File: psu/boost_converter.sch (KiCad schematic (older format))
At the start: 89 parts

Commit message: update psu
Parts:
- gave numbers to parts that had none: 89

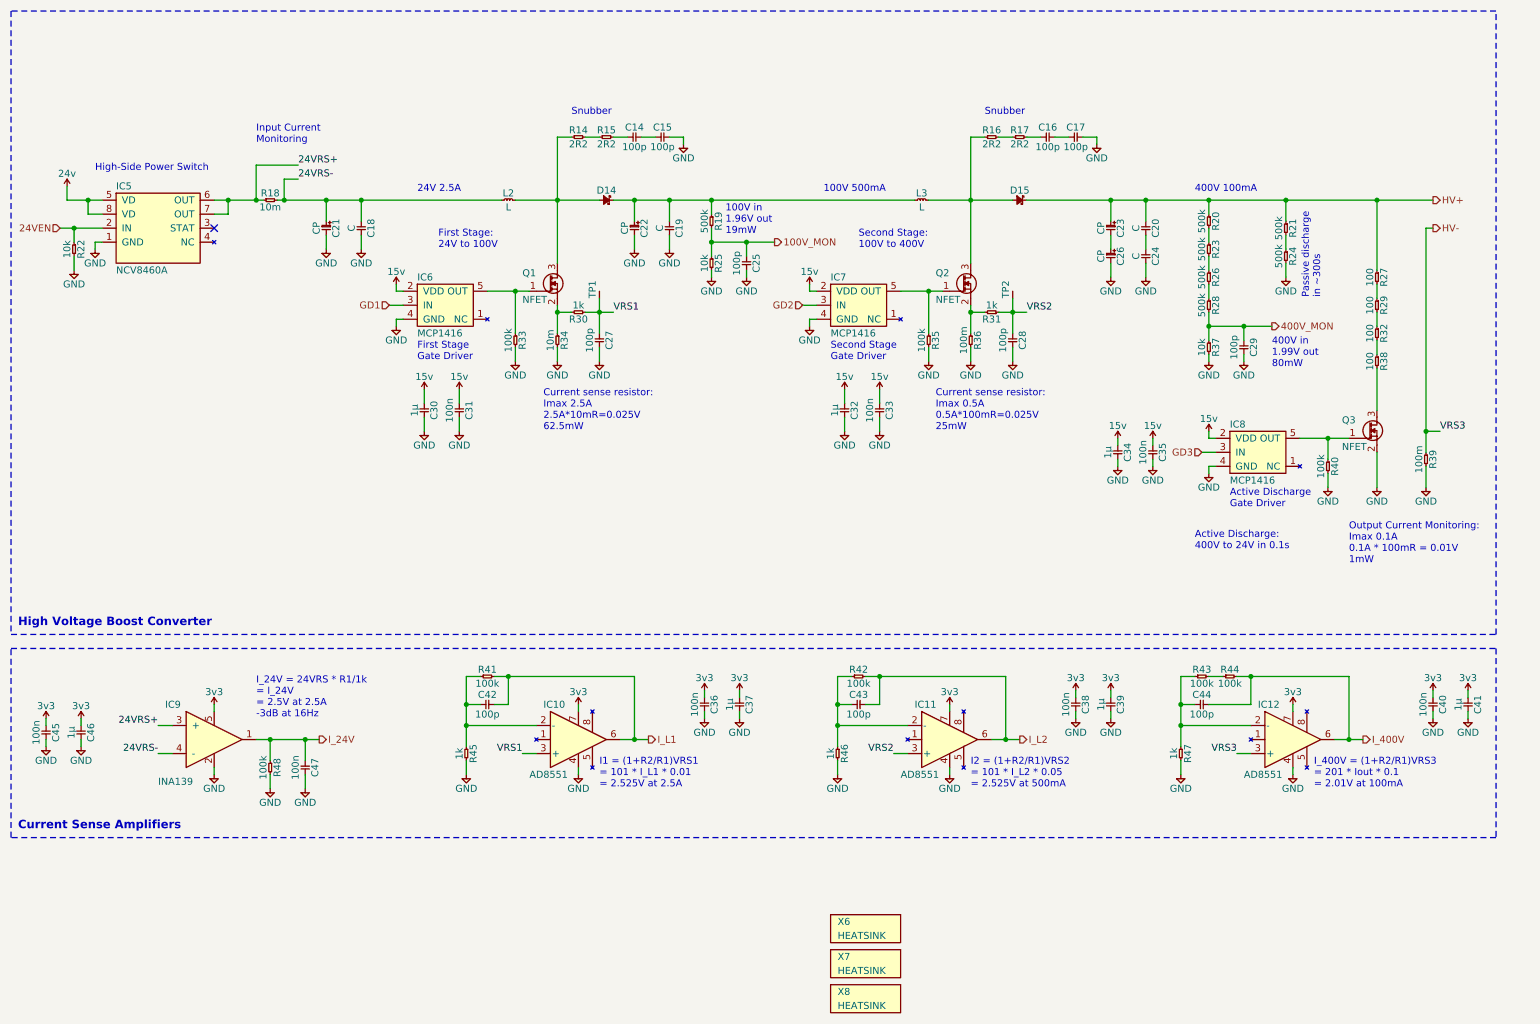
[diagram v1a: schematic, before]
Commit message: assign diodes and main transistors
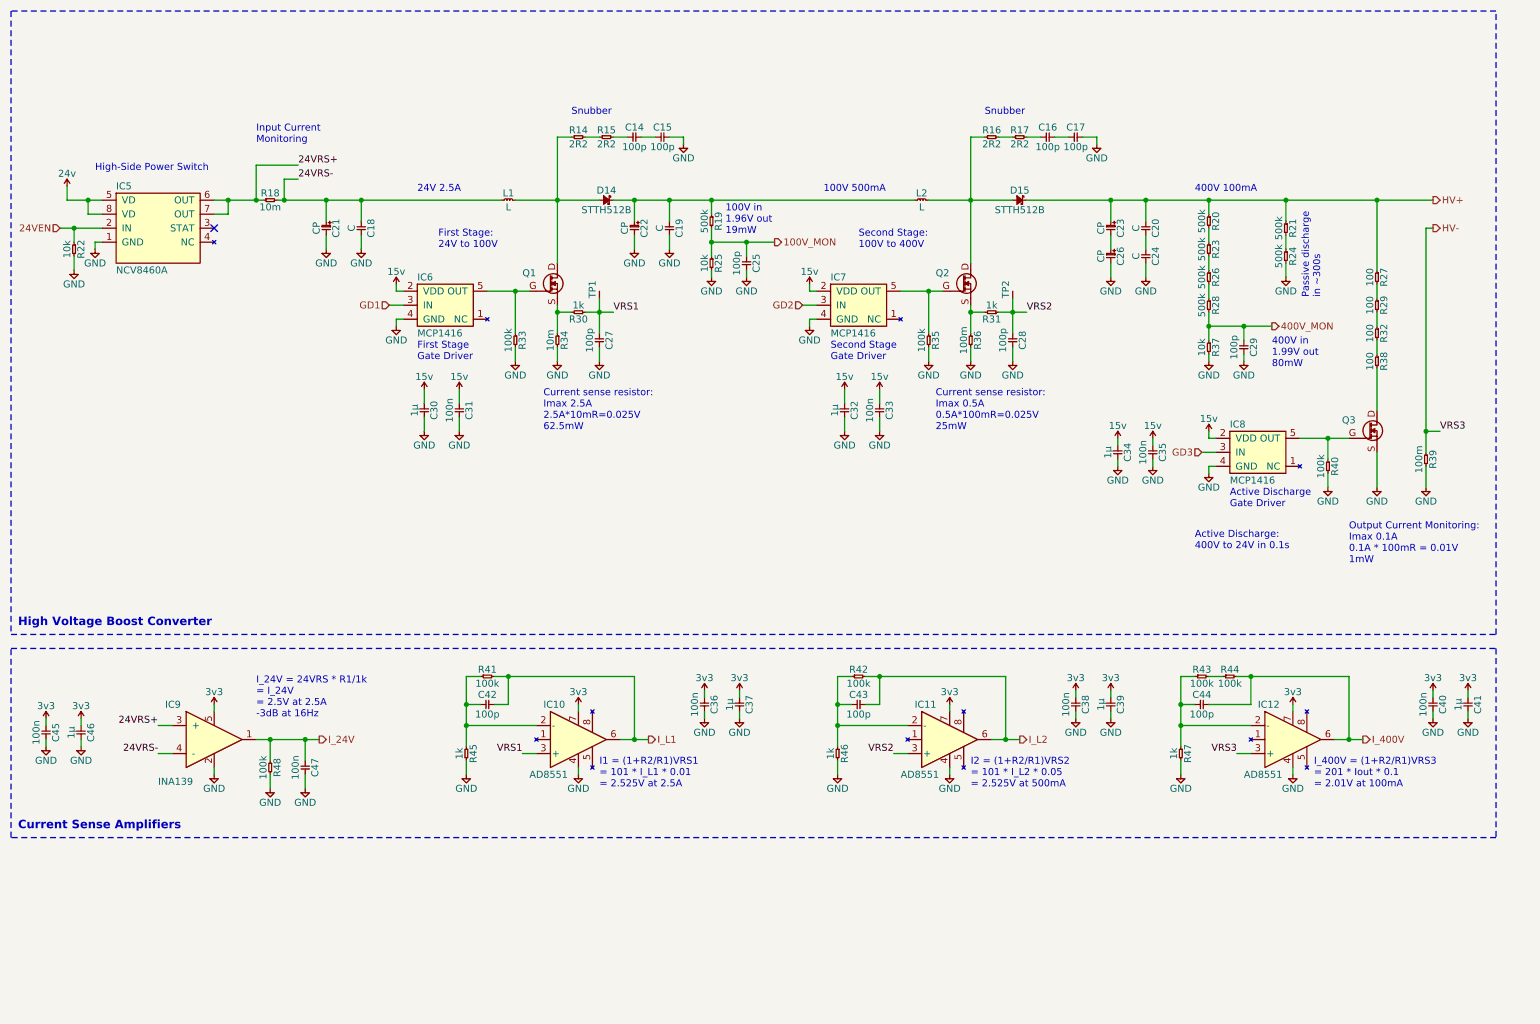
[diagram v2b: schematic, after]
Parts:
- removed Q1, Q2, Q3: NFET, symbol agg:NFET
- removed X6, X7, X8: HEATSINK, symbol agg:PART
- added Q1, Q2, Q3: STB45N60DM2AG, agg:D2PAK_GDS, symbol agg:NFET_GDS
- D14, D15: value SCHOTTKY -> STTH512B; footprint (none) -> agg:DPAK_DIODE; Farnell (none) -> 2344055
- renumbered L2 to L1, L3 to L2
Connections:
- net GND: now also Q3.S
- net at IC6.5 (OUT), R33.1: now also Q1.G
- net at IC7.5 (OUT), R35.1: now also Q2.G
- net at R30.2, R34.1: now also Q1.S
- net at D14.2, L1.2, R14.1: now also Q1.D
- net at R31.2, R36.1: now also Q2.S
- net at D15.2, L2.2, R16.1: now also Q2.D
- net at IC8.5 (OUT), R40.1: now also Q3.G
- net at R38.2: now also Q3.D
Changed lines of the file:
@@
 	6300 2650 6200 2650
-$Comp
-L agg:NFET Q?
-U 1 1 614C6078
-P 4450 2450
-AR Path="/614C6078" Ref="Q?"  Part="1"
-AR Path="/6147A5D5/614C6078" Ref="Q1"  Part="1"
-F 0 "Q1" H 4200 2480 50  0000 L CNN
-F 1 "NFET" H 4200 2290 50  0000 L CNN
-F 2 "" H 4450 2450 50  0001 C CNN
-F 3 "" H 4450 2450 50  0001 C CNN
-	1    4450 2450
-	1    0    0    -1
-$EndComp
 $Comp
 L agg:R R?
@@
 Wire Wire Line
 	4150 2550 4250 2550
-$Comp
-L agg:NFET Q?
-U 1 1 614C6088
-P 7400 2450
-AR Path="/614C6088" Ref="Q?"  Part="1"
-AR Path="/6147A5D5/614C6088" Ref="Q2"  Part="1"
-F 0 "Q2" H 7150 2480 50  0000 L CNN
-F 1 "NFET" H 7150 2290 50  0000 L CNN
-F 2 "" H 7400 2450 50  0001 C CNN
-F 3 "" H 7400 2450 50  0001 C CNN
-	1    7400 2450
-	1    0    0    -1
-$EndComp
 $Comp
 L agg:R R?
@@
 P 4050 1900
 AR Path="/614C6132" Ref="L?"  Part="1"
-AR Path="/6147A5D5/614C6132" Ref="L2"  Part="1"
-F 0 "L2" H 4100 1950 50  0000 C CNN
+AR Path="/6147A5D5/614C6132" Ref="L1"  Part="1"
+F 0 "L1" H 4100 1950 50  0000 C CNN
 F 1 "L" H 4100 1850 50  0000 C CNN
 F 2 "" H 4050 1900 50  0001 C CNN
@@
 AR Path="/6147A5D5/614C615C" Ref="D14"  Part="1"
 F 0 "D14" H 4900 1970 50  0000 C CNN
-F 1 "SCHOTTKY" H 4900 1830 50  0001 C CNN
-F 2 "" H 4800 1870 50  0001 C CNN
-F 3 "" H 4900 1970 50  0001 C CNN
+F 1 "STTH512B" H 4900 1830 50  0000 C CNN
+F 2 "agg:DPAK_DIODE" H 4800 1870 50  0001 C CNN
+F 3 "https://www.st.com/resource/en/datasheet/stth512.pdf" H 4900 1970 50  0001 C CNN
+F 4 "2344055" H 4850 1900 50  0001 C CNN "Farnell"
 	1    4850 1900
 	-1   0    0    -1
@@
 P 7000 1900
 AR Path="/614C6176" Ref="L?"  Part="1"
-AR Path="/6147A5D5/614C6176" Ref="L3"  Part="1"
-F 0 "L3" H 7050 1950 50  0000 C CNN
+AR Path="/6147A5D5/614C6176" Ref="L2"  Part="1"
+F 0 "L2" H 7050 1950 50  0000 C CNN
 F 1 "L" H 7050 1850 50  0000 C CNN
 F 2 "" H 7000 1900 50  0001 C CNN
@@
 Wire Wire Line
 	7400 1900 7100 1900
-$Comp
-L agg:SCHOTTKY D?
-U 1 1 614C617E
-P 7800 1900
-AR Path="/614C617E" Ref="D?"  Part="1"
-AR Path="/6147A5D5/614C617E" Ref="D15"  Part="1"
-F 0 "D15" H 7850 1970 50  0000 C CNN
-F 1 "SCHOTTKY" H 7850 1830 50  0001 C CNN
-F 2 "" H 7750 1870 50  0001 C CNN
-F 3 "" H 7850 1970 50  0001 C CNN
-	1    7800 1900
-	-1   0    0    -1
-$EndComp
 Wire Wire Line
 	7700 1900 7400 1900
@@
 F 4 "1630421" H 9250 3200 50  0001 L CNN "Farnell"
 	1    9450 3700
-	1    0    0    -1
-$EndComp
-$Comp
-L agg:NFET Q?
-U 1 1 614C628B
-P 10300 3500
-AR Path="/614C628B" Ref="Q?"  Part="1"
-AR Path="/6147A5D5/614C628B" Ref="Q3"  Part="1"
-F 0 "Q3" H 10050 3530 50  0000 L CNN
-F 1 "NFET" H 10050 3340 50  0000 L CNN
-F 2 "" H 10300 3500 50  0001 C CNN
-F 3 "" H 10300 3500 50  0001 C CNN
-	1    10300 3500
 	1    0    0    -1
 $EndComp
@@
 Text Notes 600  6400 0    60   ~ 12
 Current Sense Amplifiers
-$Comp
-L agg:PART X?
-U 1 1 6297628F
-P 6400 7650
-AR Path="/6297628F" Ref="X?"  Part="1"
-AR Path="/6147A5D5/6297628F" Ref="X8"  Part="1"
-F 0 "X8" H 6450 7750 50  0000 L CNN
-F 1 "HEATSINK" H 6450 7650 50  0000 L CNN
-F 2 "" H 6400 7650 50  0001 C CNN
-F 3 "" H 6400 7650 50  0001 C CNN
-	1    6400 7650
-	1    0    0    -1
-$EndComp
-$Comp
-L agg:PART X?
-U 1 1 62976295
-P 6400 7400
-AR Path="/62976295" Ref="X?"  Part="1"
-AR Path="/6147A5D5/62976295" Ref="X7"  Part="1"
-F 0 "X7" H 6450 7500 50  0000 L CNN
-F 1 "HEATSINK" H 6450 7400 50  0000 L CNN
-F 2 "" H 6400 7400 50  0001 C CNN
-F 3 "" H 6400 7400 50  0001 C CNN
-	1    6400 7400
-	1    0    0    -1
-$EndComp
-$Comp
-L agg:PART X?
-U 1 1 629A6209
-P 6400 7150
-AR Path="/629A6209" Ref="X?"  Part="1"
-AR Path="/6147A5D5/629A6209" Ref="X6"  Part="1"
-F 0 "X6" H 6450 7250 50  0000 L CNN
-F 1 "HEATSINK" H 6450 7150 50  0000 L CNN
-F 2 "" H 6400 7150 50  0001 C CNN
-F 3 "" H 6400 7150 50  0001 C CNN
-	1    6400 7150
-	1    0    0    -1
-$EndComp
 Wire Notes Line
 	550  5000 11150 5000
@@
 Wire Wire Line
 	8150 5550 8150 5600
+$Comp
+L agg:SCHOTTKY D?
+U 1 1 62C4FC38
+P 7800 1900
+AR Path="/62C4FC38" Ref="D?"  Part="1"
+AR Path="/6147A5D5/62C4FC38" Ref="D15"  Part="1"
+F 0 "D15" H 7850 1970 50  0000 C CNN
+F 1 "STTH512B" H 7850 1830 50  0000 C CNN
+F 2 "agg:DPAK_DIODE" H 7750 1870 50  0001 C CNN
+F 3 "https://www.st.com/resource/en/datasheet/stth512.pdf" H 7850 1970 50  0001 C CNN
+F 4 "2344055" H 7800 1900 50  0001 C CNN "Farnell"
+	1    7800 1900
+	-1   0    0    -1
+$EndComp
+$Comp
+L agg:NFET_GDS Q1
+U 1 1 62C5D73E
+P 4450 2450
+F 0 "Q1" H 4200 2480 50  0000 L CNN
+F 1 "STB45N60DM2AG" H 4365 2285 50  0001 R CNN
+F 2 "agg:D2PAK_GDS" H 4450 2450 50  0001 C CNN
+F 3 "https://www.st.com/resource/en/datasheet/stb45n60dm2ag.pdf" H 4450 2450 50  0001 C CNN
+F 4 "3129762" H 4450 2450 50  0001 C CNN "Farnell"
+	1    4450 2450
+	1    0    0    -1
+$EndComp
+$Comp
+L agg:NFET_GDS Q2
+U 1 1 62C5E943
+P 7400 2450
+F 0 "Q2" H 7150 2480 50  0000 L CNN
+F 1 "STB45N60DM2AG" H 7315 2285 50  0001 R CNN
+F 2 "agg:D2PAK_GDS" H 7400 2450 50  0001 C CNN
+F 3 "https://www.st.com/resource/en/datasheet/stb45n60dm2ag.pdf" H 7400 2450 50  0001 C CNN
+F 4 "3129762" H 7400 2450 50  0001 C CNN "Farnell"
+	1    7400 2450
+	1    0    0    -1
+$EndComp
+$Comp
+L agg:NFET_GDS Q3
+U 1 1 62C60334
+P 10300 3500
+F 0 "Q3" H 10050 3530 50  0000 L CNN
+F 1 "STB45N60DM2AG" H 10215 3335 50  0001 R CNN
+F 2 "agg:D2PAK_GDS" H 10300 3500 50  0001 C CNN
+F 3 "https://www.st.com/resource/en/datasheet/stb45n60dm2ag.pdf" H 10300 3500 50  0001 C CNN
+F 4 "3129762" H 10300 3500 50  0001 C CNN "Farnell"
+	1    10300 3500
+	1    0    0    -1
+$EndComp
 $EndSCHEMATC

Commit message: Select main L and C
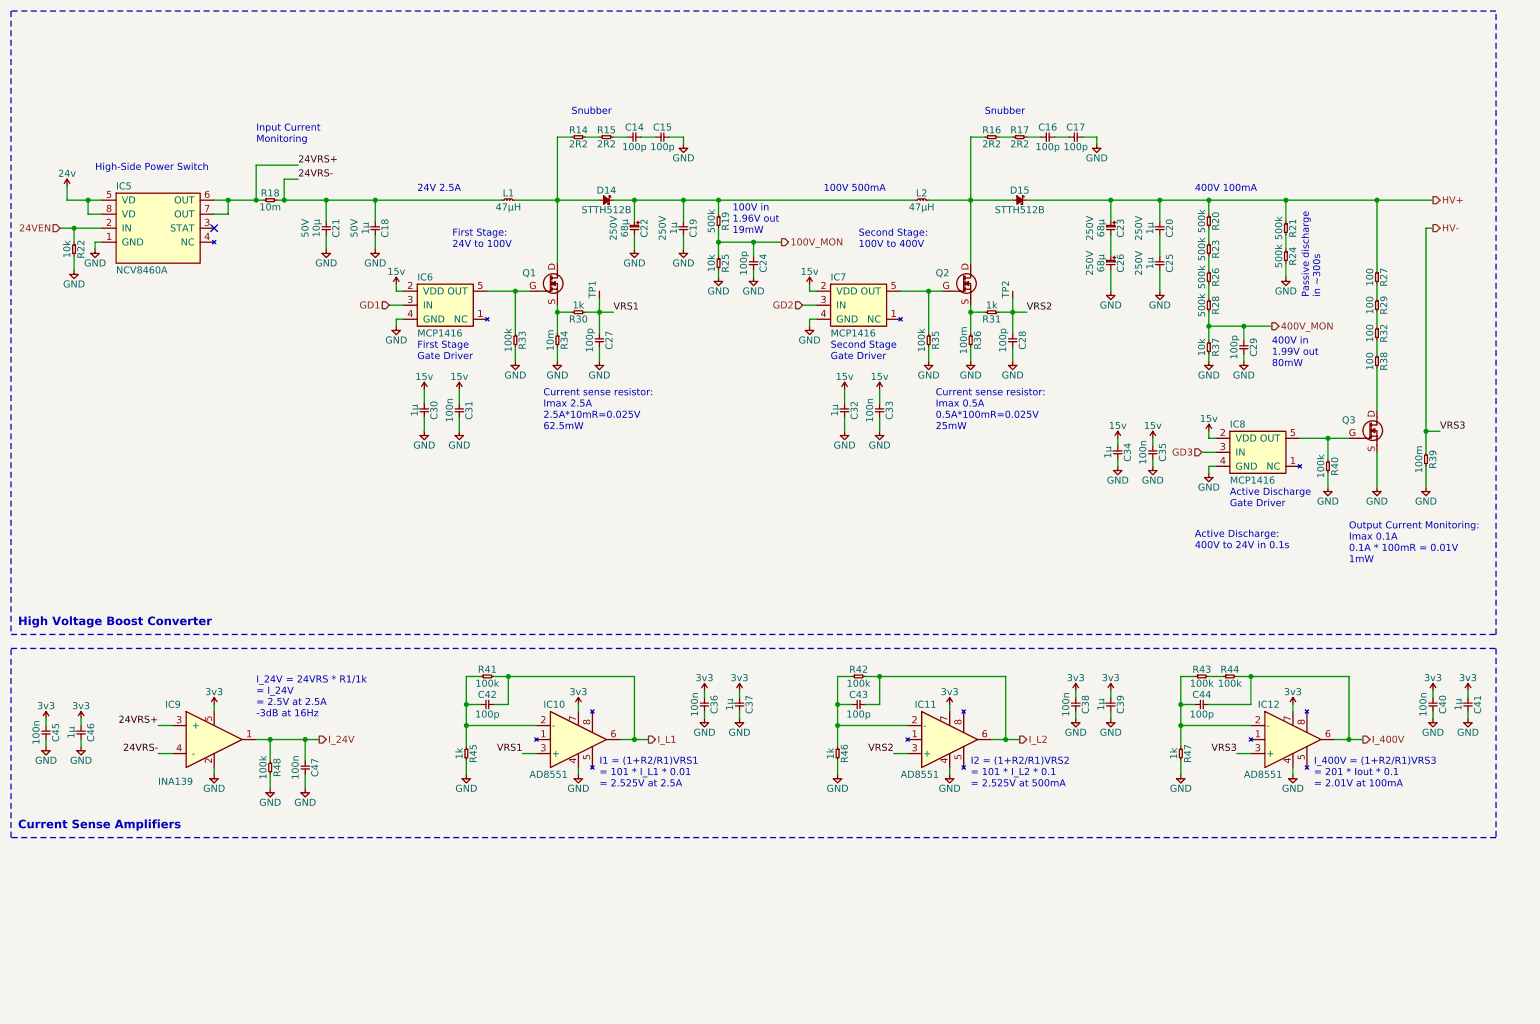
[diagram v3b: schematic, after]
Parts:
- removed C21: CP, symbol agg:CP
- removed C24: C, symbol agg:C
- added C21: 10µ, symbol agg:C
- added C25: 1µ, agg:2220, symbol agg:C
- C18: value C -> 1µ; footprint (none) -> agg:1206; Farnell (none) -> 1759454; Voltage 50 -> 50V
- C19, C20: value C -> 1µ; footprint (none) -> agg:2220; Farnell (none) -> 1828845; Voltage 250 -> 250V
- C22, C23, C26: value CP -> 68µ; Farnell (none) -> 2326343; Voltage 250 -> 250V
- L1, L2: value L -> 47µH; footprint (none) -> agg:MSS1210; Farnell (none) -> 2288335
- R27, R29, R32, R38: footprint agg:0805 -> agg:1210
- renumbered C25 to C24
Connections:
- net 24VRS-: now also C21.1
- net GND: now also C21.2, C25.2
- net at C20.2: now also C25.1
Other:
- note added: "I2 = (1+R2/R1)VRS2\n= 101 * I_L2 * 0.1\n= 2.525V at 500mA"
- note removed: "I2 = (1+R2/R1)VRS2\n= 101 * I_L2 * 0.05\n= 2.525V at 500mA"
- moved on the sheet: C18, C19, C24, R19, R25

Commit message: Update current sense Rs
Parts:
- removed C15: 100p, symbol agg:C
- removed R15: 2R2, symbol agg:R
- removed R44: 100k, agg:0603, symbol agg:R
- added C?: DNF, agg:0805, symbol agg:C
- added R? (x2): 100k, agg:0805, symbol agg:R
- added R? (x3): 1k, agg:0603, symbol agg:R
- added R?: DNF, agg:0805, symbol agg:R
- C14, C16, C17: value 100p -> DNF; footprint (none) -> agg:0805
- R14, R16, R17: value 2R2 -> DNF; footprint (none) -> agg:0805
- R21, R24: value 500k -> 100k
- R36, R39: value 100m -> 10m
- R41, R42: value 100k -> 68k
- R43: value 100k -> 1M
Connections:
- net GND: now also C14.2, C?.2, R?.2; no longer C17.2, R24.2
- net HV-: now also R?.2; no longer IC12.3 (+)
- net I_400V: now also R43.2
- net VRS1: now also R?.2; no longer IC10.3 (+)
- net VRS2: now also R?.2; no longer IC11.3 (+)
- net at R14.2: now also C14.1
- net at R17.2: now also R?.1; no longer C16.1
- new net: C17.2, C?.1
- new net: C16.1, R?.2
- new net: R24.2, R?.1
- new net: IC12.3 (+), R?.1
- new net: IC11.3 (+), R?.1
- new net: IC10.3 (+), R?.1
- new net: R?.1, R?.2
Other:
- note added: "Active Discharge\nto 24V in 0.1s"
- note added: "Current sense resistor:\nImax 4.5A\n4.5A*10mR=45mV\nPmax=202mW"
- note added: "I_400V = (1+R2/R1)VRS3\n= 1001 * 1mV\n= 1.01V at 100mA"
- note added: "I_L1 = (1+R2/R1)VRS1\n= 69 * 0.045\n= 3.105V at 4.5A"
- note added: "I_L2 = (1+R2/R1)VRS2\n= 69 * 0.045\n= 3.105V at 4.5A"
- note added: "Isat=4.5A"
- note added: "Output Current Monitoring:\nImax 0.1A\n0.1A * 10mR = 1mV\nPmax 0.1mW"
- note added: "Passive discharge\nto 24V in ~~80s"
- note added: "Place and orient both\n1k resistors together"
- note removed: "Active Discharge:\n400V to 24V in 0.1s"
- note removed: "Current sense resistor:\nImax 0.5A\n0.5A*100mR=0.025V\n25mW"
- note removed: "Current sense resistor:\nImax 2.5A\n2.5A*10mR=0.025V\n62.5mW"
- note removed: "I1 = (1+R2/R1)VRS1\n= 101 * I_L1 * 0.01\n= 2.525V at 2.5A"
- note removed: "I2 = (1+R2/R1)VRS2\n= 101 * I_L2 * 0.1\n= 2.525V at 500mA"
- note removed: "I_400V = (1+R2/R1)VRS3\n= 201 * Iout * 0.1\n= 2.01V at 100mA"
- note removed: "Output Current Monitoring:\nImax 0.1A\n0.1A * 100mR = 0.01V\n1mW"
- note removed: "Passive discharge\nin ~~300s"
- moved on the sheet: C14, C16, C17, C20, C23, C25, C26, C29, C34, C35, C38, C39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
